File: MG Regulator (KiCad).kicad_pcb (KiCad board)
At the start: 2 copper layers, 50.5 x 61 mm, 17 parts, among them J1 10K thermistor connector, Q1 IRLML2060, T1 B+, T2 +, T3 -, T4 F, U1 AP7370-50FDC, U2 ACS723LLCTR-10AU-T

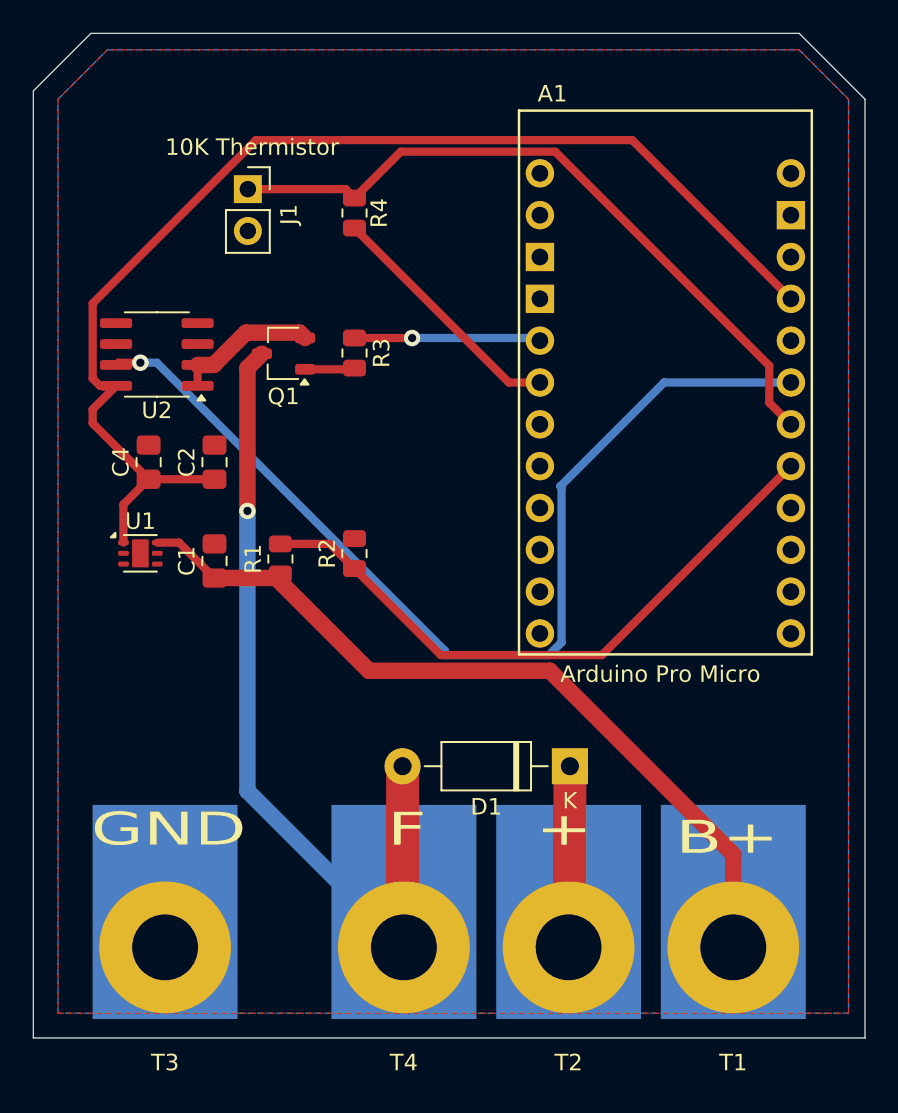
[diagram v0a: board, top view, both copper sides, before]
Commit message: Lastest vesion with switch to turn on LED when ignition turns on.
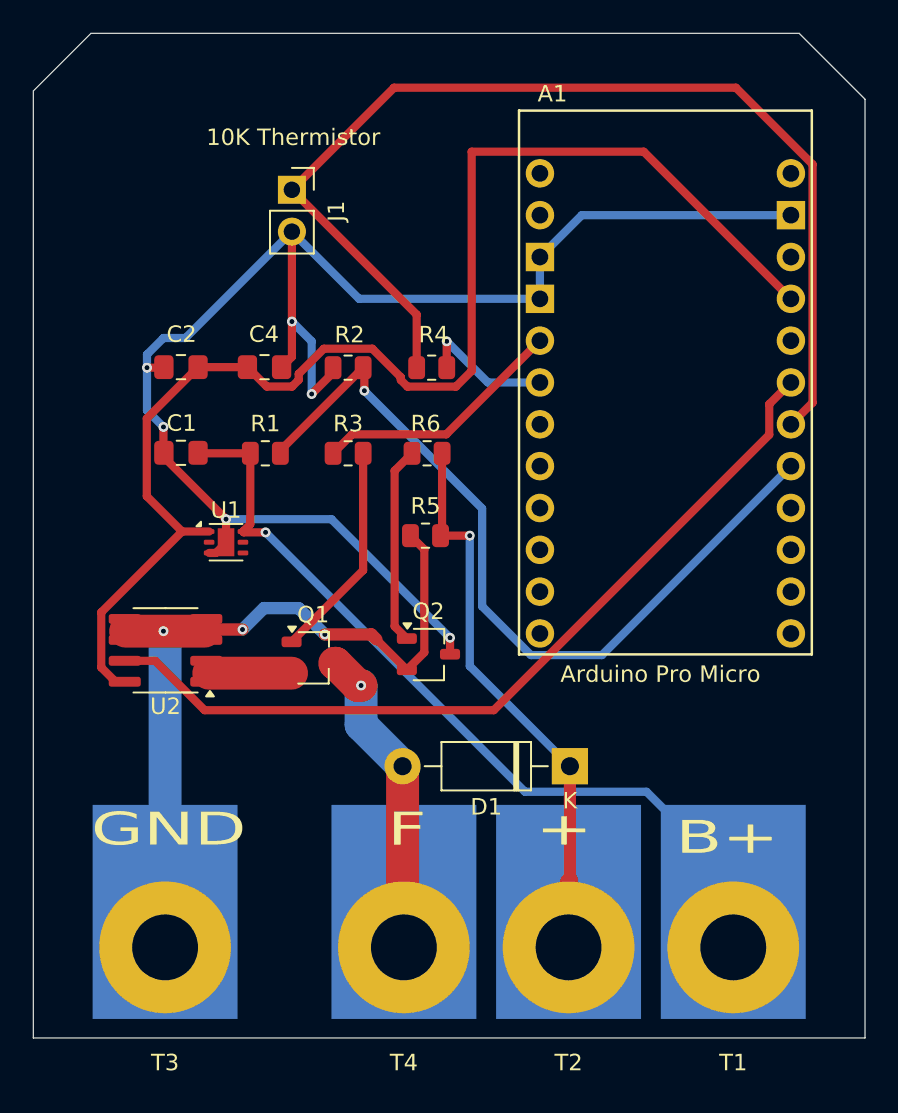
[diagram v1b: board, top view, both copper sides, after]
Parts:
- added Q2: AM2336N-CT, Package_TO_SOT_SMD:TSOT-23, F.Cu at (102.5, 112.2)
- added R5: R, Resistor_SMD:R_0805_2012Metric, F.Cu at (102.3, 105.0)
- added R6: R, Resistor_SMD:R_0805_2012Metric, F.Cu at (102.4, 100.0)
- C1, C4: value C -> 1.0uF
- D1: value 1N4002 -> 1N4005
- Q1: value IRLML2060 -> AM2336N-CT
- R1: value R -> 36K
- R2: value R -> 15K
- moved Q1 18.5 mm to (95.5, 112.4), turned to 0 degrees
- moved U2 18.0 mm to (86.5, 112.0)
- moved R2 11.3 mm to (97.6, 94.8), turned to 180 degrees
- moved R4 10.5 mm to (102.7, 94.8), turned to 180 degrees
- moved C4 9.10 mm to (92.5, 94.8), turned to 0 degrees
- moved C1 6.88 mm to (87.5, 100.0), turned to 180 degrees
- moved R1 6.48 mm to (92.6, 100.0), turned to 0 degrees
- moved C2 6.12 mm to (87.5, 94.8), turned to 180 degrees
- moved R3 6.10 mm to (97.6, 100.0), turned to 0 degrees
- moved U1 5.24 mm to (90.2, 105.4)
- moved J1 2.68 mm to (94.2, 84.0)
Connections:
- net Net-(A1-A2/D20) renamed /FLD_I_SENSE
- net Net-(D1-A) renamed /FIELD_COIL
- net Net-(D1-K) renamed /B+
- net Net-(Q1-S) renamed /FIELD_LOW1
- A1 pad GND1: GND -> /SWGND
- A1 pad GND2: GND -> /SWGND
- A1 pad GND3: GND -> /SWGND
- C1 pad 2: GND -> /SWGND
- C2 pad 2: GND -> /SWGND
- C4 pad 2: GND -> /SWGND
- J1 pad 2: GND -> /SWGND
- R2 pad 2: GND -> /SWGND
- U1 pad 3: GND -> /SWGND
- U1 pad 7: GND -> /SWGND
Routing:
- net /SWGND: track 0.00 -> 96.3 mm, vias 0 -> 6
- net GND: track 0.00 -> 51.8 mm, vias 0 -> 3
- net /FIELD_COIL: track 51.4 -> 19.1 mm
- net /B+: track 11.0 -> 37.5 mm, vias 0 -> 1
- net Net-(A1-A1/D19): track 42.5 -> 66.4 mm
- net Net-(Q2-G): track 0.00 -> 12.0 mm
- net Net-(A1-A0/D18): track 38.5 -> 49.5 mm, vias 0 -> 1
- net Net-(Q1-G): track 3.04 -> 13.2 mm
- net /FLD_I_SENSE: track 61.0 -> 51.0 mm, vias 1 -> 0
- net /VCC: track 72.8 -> 82.0 mm
- net Net-(A1-D3/SCL): track 15.1 -> 8.30 mm, vias 0 -> 1
- net Net-(A1-D2/SDA): track 11.4 -> 15.4 mm, vias 1 -> 0
- net /FIELD_LOW1: track 8.74 -> 5.24 mm
- net Net-(U1-VI): track 48.8 -> 48.7 mm, vias 0 -> 1
- removed copper zone on B.Cu, net GND
- removed copper zone on F.Cu, net GND

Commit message: Modified to be able to control the ignition led and enable arduino power from the ignition switch.
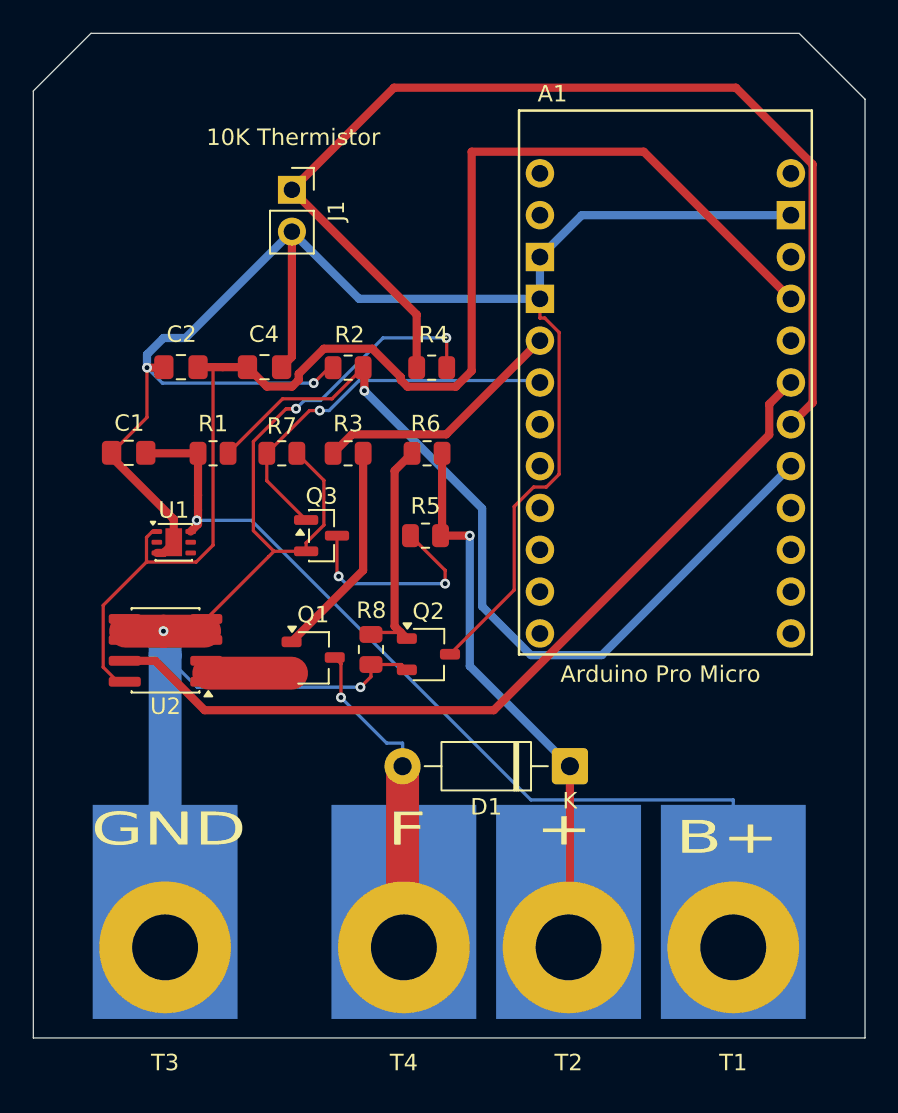
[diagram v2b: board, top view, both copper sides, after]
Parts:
- added Q3: 2N7002, Package_TO_SOT_SMD:SOT-23, F.Cu at (96.0, 105.0)
- added R7: 100K, Resistor_SMD:R_0805_2012Metric, F.Cu at (93.6, 100.0)
- added R8: 1M, Resistor_SMD:R_0805_2012Metric, F.Cu at (99.0, 111.9)
- R3: value R -> 220
- R5: value R -> 1k
- R6: value R -> 1K
- moved C1 3.18 mm to (84.3, 100.0)
- moved R1 3.18 mm to (89.4, 100.0)
- moved U1 3.17 mm to (87.0, 105.4)
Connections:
- net /B+ renamed /IGN_SW
- A1 pad D3: Net-(A1-D3/SCL) -> /WARN_LED_CTL
- R4 pad 1: Net-(A1-D3/SCL) -> GND
- R5 pad 2: GND -> Net-(Q3-D)
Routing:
- net GND: track 51.8 -> 86.5 mm, vias 3 -> 4
- net /WARN_LED_CTL: track 0.00 -> 23.5 mm, vias 0 -> 1
- net /SWGND: track 96.3 -> 109.7 mm, vias 6 -> 2
- net Net-(Q3-D): track 0.00 -> 12.9 mm, vias 0 -> 2
- net Net-(U1-VI): track 48.7 -> 57.4 mm
- net Net-(A1-D3/SCL): track 8.30 -> 0.00 mm, vias 1 -> 0
- net Net-(A1-A0/D18): track 49.5 -> 52.6 mm
- net /FIELD_COIL: track 19.1 -> 22.1 mm
- net /IGN_SW: track 37.5 -> 39.7 mm
- net Net-(Q2-G): track 12.0 -> 13.9 mm
- net /FIELD_LOW1: track 5.24 -> 6.42 mm
- net /VCC: track 82.0 -> 82.8 mm

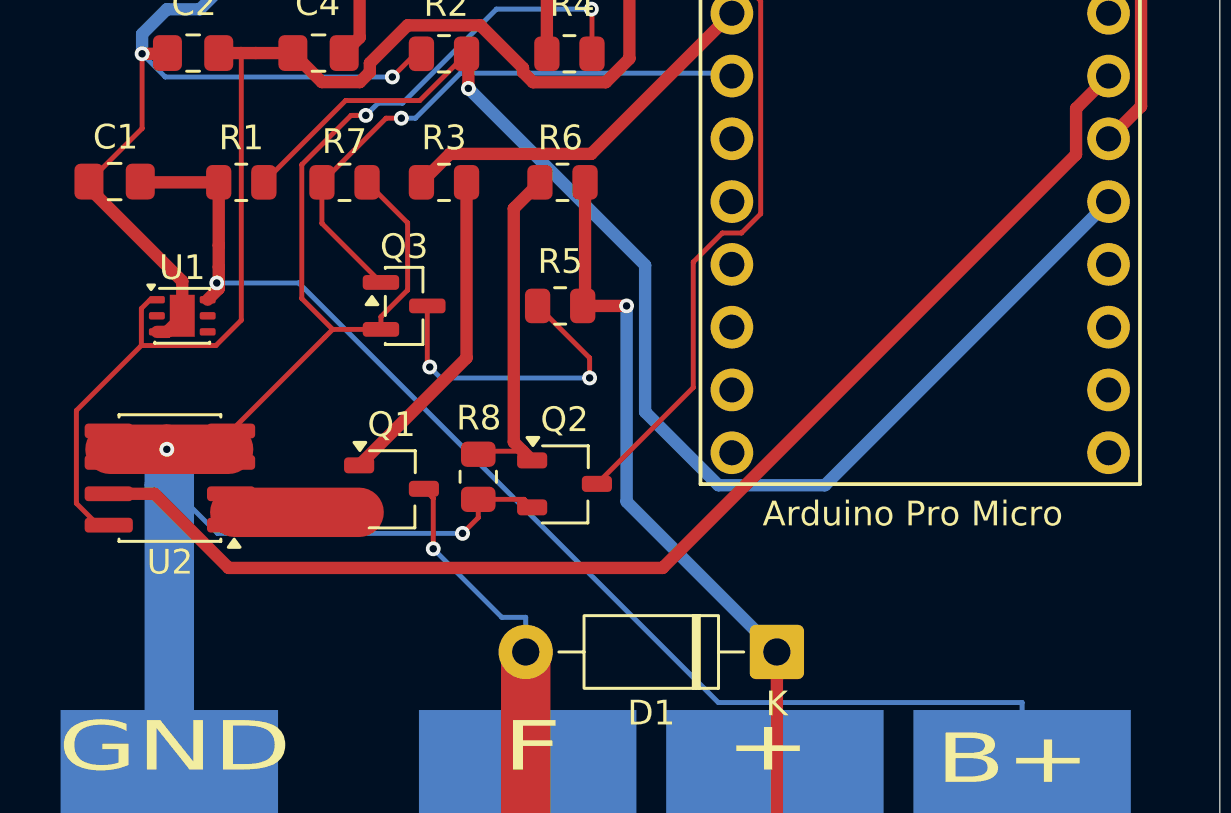
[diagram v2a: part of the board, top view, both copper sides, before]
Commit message: Minor trace width changes before ordering at JLCPCB.
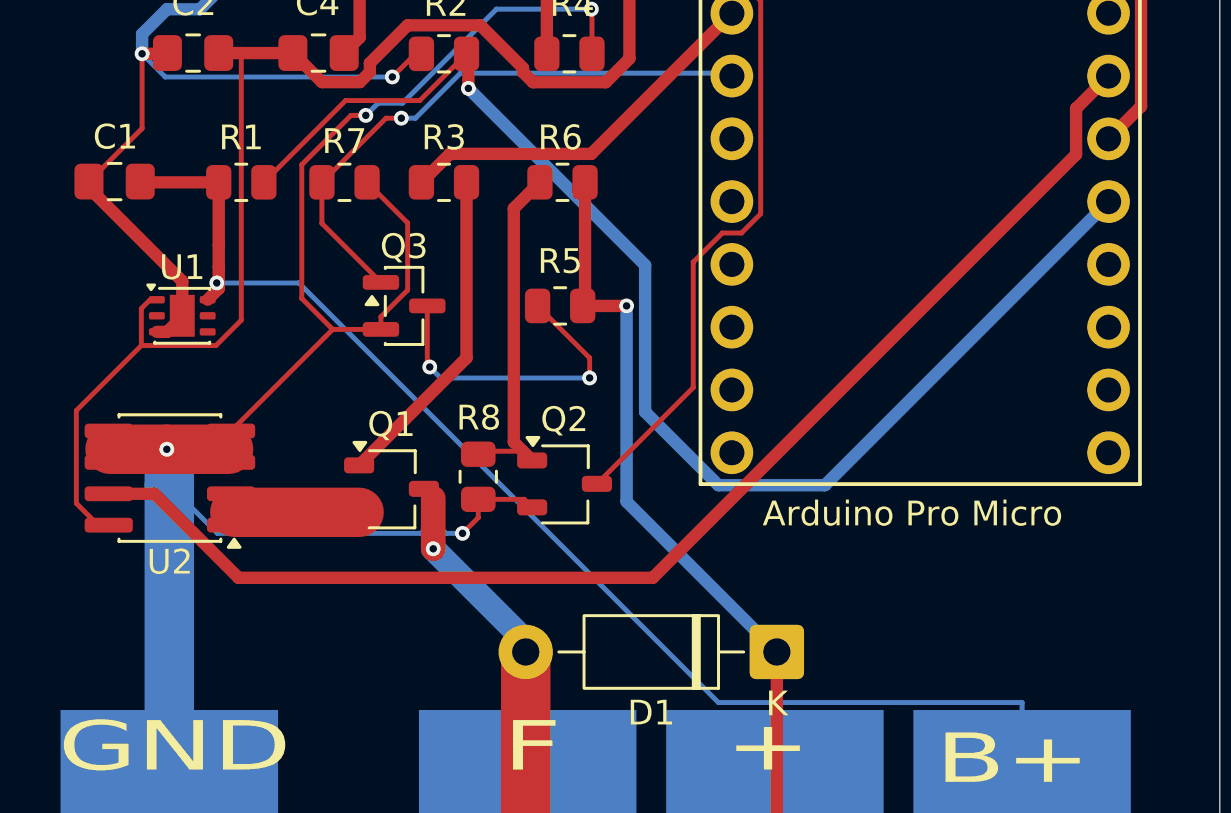
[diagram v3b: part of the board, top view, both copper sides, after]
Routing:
- net /FIELD_COIL: track 22.1 -> 21.0 mm

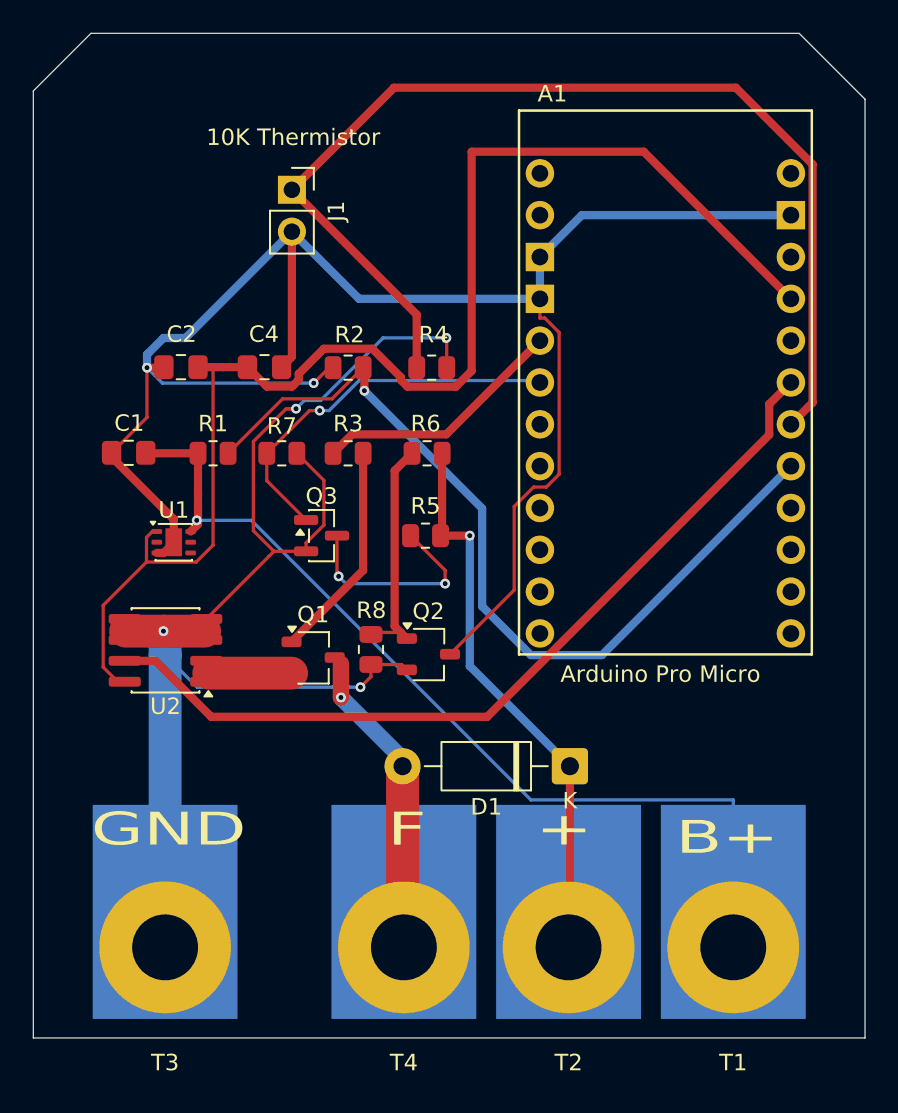
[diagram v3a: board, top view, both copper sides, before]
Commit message: Changed the fets to be the same.  Fixed the problem with the thermistor not being powered.  (this fix isn't on the boards ordered)
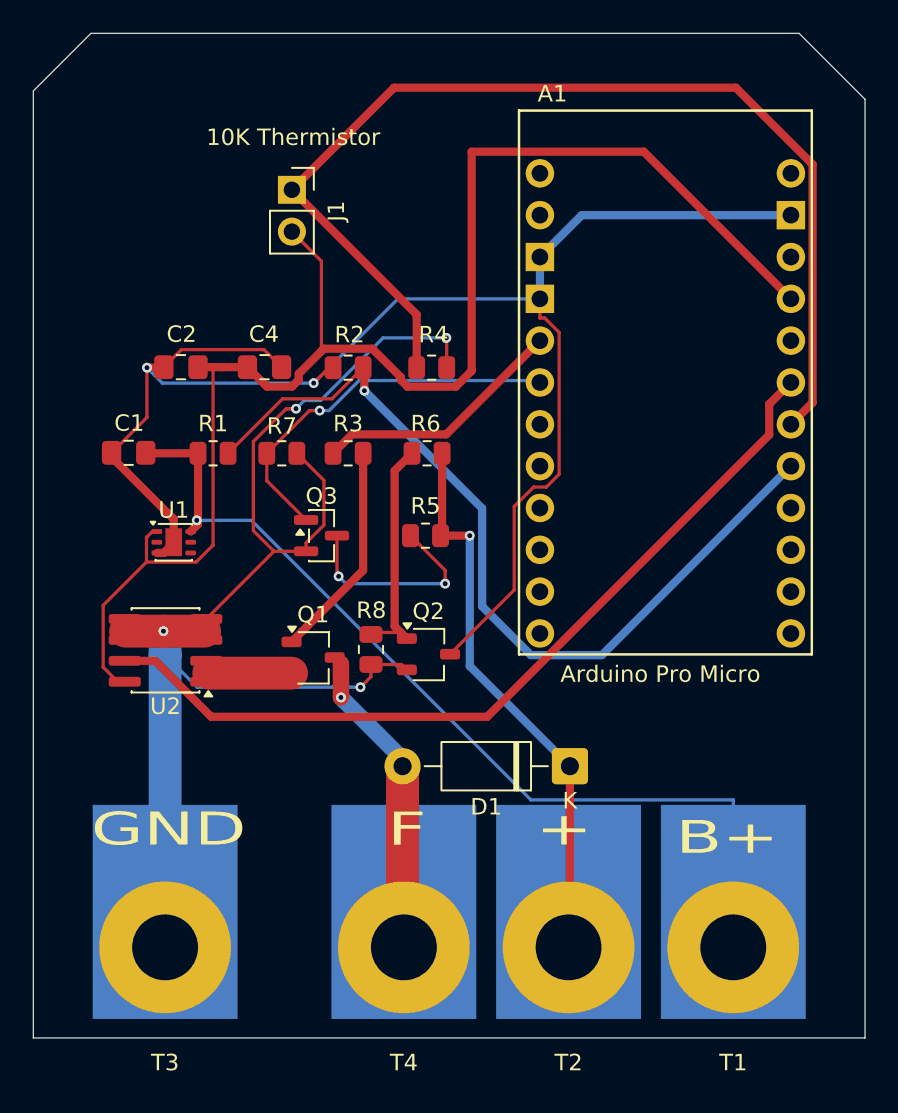
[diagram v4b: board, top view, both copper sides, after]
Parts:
- A1: value Arduino_Pro_Mini_Socket -> Arduino_Pro_Micro_Socket
- Q1, Q2: value AM2336N-CT -> DMG3414U-7
- Q3: value 2N7002 -> DMG3414U-7
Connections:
- J1 pad 2: /SWGND -> /VCC
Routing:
- net /SWGND: track 109.7 -> 95.7 mm
- net /VCC: track 82.8 -> 90.8 mm
- net /IGN_SW: track 39.7 -> 36.5 mm
- net /FIELD_COIL: track 21.0 -> 22.0 mm
